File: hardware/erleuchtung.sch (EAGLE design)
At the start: 5 parts, among them IC1 MEGA323-P

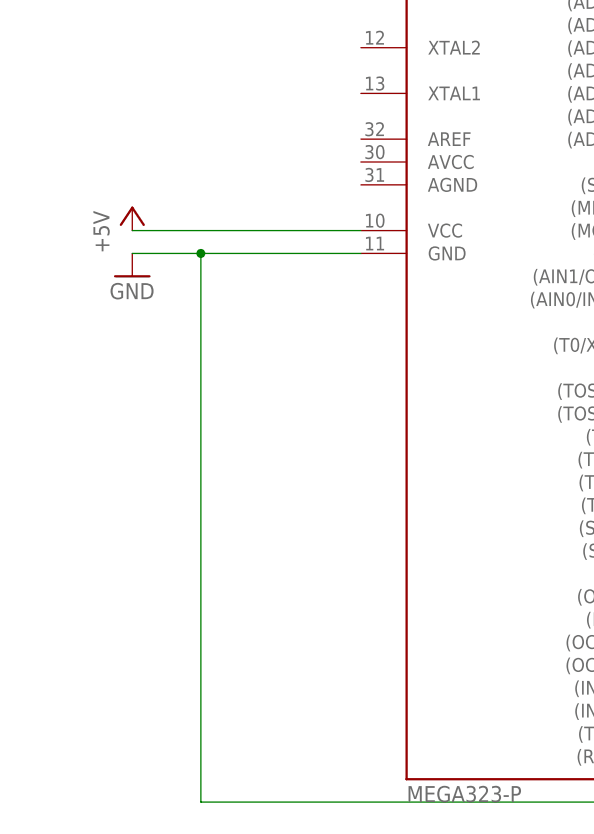
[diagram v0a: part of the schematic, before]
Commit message: wired AVCC and AGND
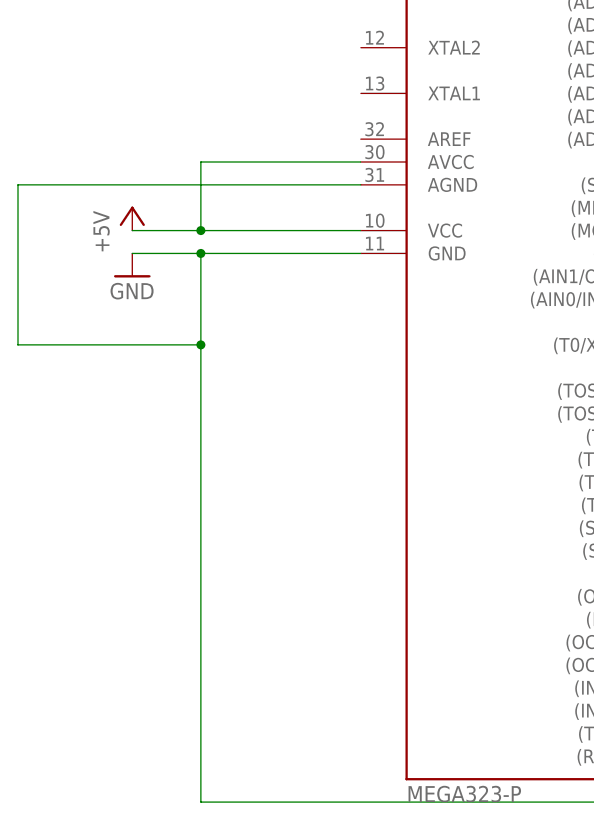
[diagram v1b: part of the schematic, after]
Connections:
- net +5V: now also IC1.AVCC
- net GND: now also IC1.AGND
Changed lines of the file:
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@@
 <wire x1="30.48" y1="55.88" x2="12.7" y2="55.88" width="0.1524" layer="91"/>
 <wire x1="12.7" y1="55.88" x2="5.08" y2="55.88" width="0.1524" layer="91"/>
-<wire x1="12.7" y1="55.88" x2="12.7" y2="-5.08" width="0.1524" layer="91"/>
+<wire x1="12.7" y1="55.88" x2="12.7" y2="45.72" width="0.1524" layer="91"/>
 <junction x="12.7" y="55.88"/>
+<wire x1="12.7" y1="45.72" x2="12.7" y2="-5.08" width="0.1524" layer="91"/>
 <wire x1="12.7" y1="-5.08" x2="121.92" y2="-5.08" width="0.1524" layer="91"/>
 <wire x1="121.92" y1="-5.08" x2="121.92" y2="53.34" width="0.1524" layer="91"/>
@@
 <wire x1="121.92" y1="53.34" x2="99.06" y2="53.34" width="0.1524" layer="91"/>
 <wire x1="99.06" y1="53.34" x2="99.06" y2="12.7" width="0.1524" layer="91"/>
+<pinref part="IC1" gate="G$1" pin="AGND"/>
+<wire x1="30.48" y1="63.5" x2="-7.62" y2="63.5" width="0.1524" layer="91"/>
+<wire x1="-7.62" y1="63.5" x2="-7.62" y2="45.72" width="0.1524" layer="91"/>
+<wire x1="-7.62" y1="45.72" x2="12.7" y2="45.72" width="0.1524" layer="91"/>
+<junction x="12.7" y="45.72"/>
 </segment>
 </net>
@@
 <segment>
 <pinref part="IC1" gate="G$1" pin="VCC"/>
-<wire x1="30.48" y1="58.42" x2="5.08" y2="58.42" width="0.1524" layer="91"/>
+<wire x1="30.48" y1="58.42" x2="12.7" y2="58.42" width="0.1524" layer="91"/>
 <pinref part="P+1" gate="1" pin="+5V"/>
+<pinref part="IC1" gate="G$1" pin="AVCC"/>
+<wire x1="12.7" y1="58.42" x2="5.08" y2="58.42" width="0.1524" layer="91"/>
+<wire x1="30.48" y1="66.04" x2="12.7" y2="66.04" width="0.1524" layer="91"/>
+<wire x1="12.7" y1="66.04" x2="12.7" y2="58.42" width="0.1524" layer="91"/>
+<junction x="12.7" y="58.42"/>
 </segment>
 </net>
